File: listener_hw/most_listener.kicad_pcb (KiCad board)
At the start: 2 copper layers, 125 x 80 mm, 153 parts, among them J1 1-1394640-1, J2 ANALYSER, J3 I2S, J4 VBAT_IN, J5 PLR135/T10, J6 PLT133/T10W, J7 RCA 75R, J8 LINE L, J9 LINE R, M1 Tang Nano 20K, M2 ESP32-DevKitC-VIE, U1 74LVC1G34, U10 TPS2553DBVR, U11 74LVC1G123, U12 DIR9001, U13 SRC4192, U14 LP5907MFX-3.3, U15 PCM5102A, U16 LP5907MFX-3.3, U2 74LVC1G157, U3 74LVC1G125, U4 74LVC1G123, U5 TPS7B8133DRV, U6 LMR38020F, U7 Si514, U8 LP5907MFX-3.3, U9 74LVC1G79, X1 24.576MHz

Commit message: Board v1.3: the TOSLINK input's AUDIO flag to the host and the ASRC's RDY to its MUTE; the audio-in source chosen by itself
- firmware: the source picks itself (components/mostctl/ain): the phone while it streams,
  otherwise the TOSLINK input once its receiver has held lock on PCM for 1 s; a parity
  error's blip is kept, 100 ms of ERROR loses it; its lock time runs while the phone plays;
  key i gone
- the DIR9001 passes non-PCM (AC-3, DTS) to DOUT untouched (SLES198A 8.3.9.2): its AUDIO pin,
  channel-status bit 1, now reaches M2 IO27 (OPT_NPCM, pulled up); high drops the TOSLINK input
  at the first reading, and the console says to set the source to PCM
- the SRC4192's RDY drives its MUTE, which no longer sits on ground (SBFS022C 7.3.5): silent
  while its rate estimator settles on a new rate
- sheet: AUDIO on U12's left side, MUTE on U13's right side under RDY; the host block's text
  fitted into its frame; J5's value moved clear of OPT_NPCM; rev 1.3
- board: pads from the sheet, U13.14's ground via gone; RDY-MUTE one jumper, 1.4 mm under U13
  across RST_AIN; OPT_NPCM from U12.1 to M2.11 with three - 1.0 and 1.4 mm at M2, whose pad 11
  is walled in by I2S_DIN2_F and SRC_LRCK_F, and 3.8 mm at U12 across OPT_ERR and RST_AIN;
  37 jumpers, 83 mm in all, the longest still 6.8 mm; "v1.3" in the silk
- checks: DRC no error, no warning, nothing unconnected, matches the sheet; ERC clean; the
  firmware's pins agree with the netlist; host tests (seven broken variants of ain.c each
  caught); ESP-IDF build 979 KB, no warnings; check_all --quick 24/24

Co-Authored-By: Claude Opus 5.5 <noreply@anthropic.com>
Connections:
- M2 pad 11: unconnected-(M2-IO27-Pad11) -> /OPT_NPCM
- U12 pad 1: unconnected-(U12-AUDIO-Pad1) -> /OPT_NPCM
- U13 pad 14: GND -> Net-(U13-MUTE)
- U13 pad 15: unconnected-(U13-RDY-Pad15) -> Net-(U13-MUTE)
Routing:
- net /OPT_NPCM: track 0.00 -> 24.3 mm, vias 0 -> 5
- net Net-(U13-MUTE): track 0.00 -> 5.86 mm, vias 0 -> 2
- net GND: track 153.3 -> 152.2 mm, vias 336 -> 335
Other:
- board text added: "v1.3"
- board text removed: "v1.2"
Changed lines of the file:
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@@
 		(title "MOST25 to AUDIO: listener board")
 		(date "2026-09-28")
-		(rev "1.2")
+		(rev "1.3")
 		(comment 1 "Generated sheet: listener_hw/gen_listener.py")
 	)
@@
 			(layers "*.Cu" "*.Mask")
 			(remove_unused_layers no)
-			(net "unconnected-(M2-IO27-Pad11)")
+			(net "/OPT_NPCM")
 		)
 		(pad "12" thru_hole circle
@@
 			(layers "F.Cu" "F.Mask" "F.Paste")
 			(roundrect_rratio 0.25)
-			(net "unconnected-(U12-AUDIO-Pad1)")
+			(net "/OPT_NPCM")
 		)
 		(pad "2" smd roundrect
@@
 			(layers "F.Cu" "F.Mask" "F.Paste")
 			(roundrect_rratio 0.25)
-			(net "GND")
+			(net "Net-(U13-MUTE)")
 		)
 		(pad "15" smd roundrect
@@
 			(layers "F.Cu" "F.Mask" "F.Paste")
 			(roundrect_rratio 0.25)
-			(net "unconnected-(U13-RDY-Pad15)")
+			(net "Net-(U13-MUTE)")
 		)
 		(pad "16" smd roundrect
@@
 		)
 	)
-	(gr_text "v1.2"
+	(gr_text "v1.3"
 		(at 112.5 3.2 0)
 		(layer "F.SilkS")
@@
 	)
 	(segment
-		(start 95.75 18.775)
-		(end 96.490049 17.881654)
-		(width 0.35)
-		(locked yes)
-		(layer "F.Cu")
-		(net "GND")
-	)
-	(segment
 		(start 9 10)
 		(end 10.4 10)
@@
 	)
 	(via
-		(at 96.490049 17.881654)
-		(size 0.6)
-		(drill 0.3)
-		(layers "F.Cu" "B.Cu")
-		(locked yes)
-		(net "GND")
-	)
-	(via
 		(at 100.199999 14.2)
 		(size 0.6)
@@
 	)
 	(segment
+		(start 86.1 19.8)
+		(end 86.1 16.6)
+		(width 0.25)
+		(locked yes)
+		(layer "F.Cu")
+		(net "/OPT_NPCM")
+	)
+	(segment
+		(start 85.4 22)
+		(end 85.4 20.9)
+		(width 0.25)
+		(locked yes)
+		(layer "F.Cu")
+		(net "/OPT_NPCM")
+	)
+	(segment
+		(start 99.1 16.1)
+		(end 99.6 16.6)
+		(width 0.25)
+		(locked yes)
+		(layer "F.Cu")
+		(net "/OPT_NPCM")
+	)
+	(segment
+		(start 99.6 16.6)
+		(end 99.9 16.6)
+		(width 0.25)
+		(locked yes)
+		(layer "F.Cu")
+		(net "/OPT_NPCM")
+	)
+	(segment
+		(start 98.5 14.9)
+		(end 99.1 15.5)
+		(width 0.25)
+		(locked yes)
+		(layer "F.Cu")
+		(net "/OPT_NPCM")
+	)
+	(segment
+		(start 86.1 16.6)
+		(end 89.9 12.8)
+		(width 0.25)
+		(locked yes)
+		(layer "F.Cu")
+		(net "/OPT_NPCM")
+	)
+	(segment
+		(start 95 12.8)
+		(end 95.4 13.2)
+		(width 0.25)
+		(locked yes)
+		(layer "F.Cu")
+		(net "/OPT_NPCM")
+	)
+	(segment
+		(start 99.1 15.5)
+		(end 99.1 16.1)
+		(width 0.25)
+		(locked yes)
+		(layer "F.Cu")
+		(net "/OPT_NPCM")
+	)
+	(segment
+		(start 89.9 12.8)
+		(end 95 12.8)
+		(width 0.25)
+		(locked yes)
+		(layer "F.Cu")
+		(net "/OPT_NPCM")
+	)
+	(segment
+		(start 85.2 22.2)
+		(end 85.4 22)
+		(width 0.25)
+		(locked yes)
+		(layer "F.Cu")
+		(net "/OPT_NPCM")
+	)
+	(via
+		(at 98.5 14.9)
+		(size 0.6)
+		(drill 0.3)
+		(layers "F.Cu" "B.Cu")
+		(locked yes)
+		(net "/OPT_NPCM")
+	)
+	(via
+		(at 85.4 20.9)
+		(size 0.6)
+		(drill 0.3)
+		(layers "F.Cu" "B.Cu")
+		(locked yes)
+		(net "/OPT_NPCM")
+	)
+	(via
+		(at 86.1 19.8)
+		(size 0.6)
+		(drill 0.3)
+		(layers "F.Cu" "B.Cu")
+		(locked yes)
+		(net "/OPT_NPCM")
+	)
+	(via
+		(at 85.2 22.2)
+		(size 0.6)
+		(drill 0.3)
+		(layers "F.Cu" "B.Cu")
+		(locked yes)
+		(net "/OPT_NPCM")
+	)
+	(via
+		(at 95.4 13.2)
+		(size 0.6)
+		(drill 0.3)
+		(layers "F.Cu" "B.Cu")
+		(locked yes)
+		(net "/OPT_NPCM")
+	)
+	(segment
+		(start 84.5 22.9)
+		(end 85.2 22.2)
+		(width 0.25)
+		(locked yes)
+		(layer "B.Cu")
+		(net "/OPT_NPCM")
+	)
+	(segment
+		(start 85.4 20.5)
+		(end 86.1 19.8)
+		(width 0.25)
+		(locked yes)
+		(layer "B.Cu")
+		(net "/OPT_NPCM")
+	)
+	(segment
+		(start 85.4 20.9)
+		(end 85.4 20.5)
+		(width 0.25)
+		(locked yes)
+		(layer "B.Cu")
+		(net "/OPT_NPCM")
+	)
+	(segment
+		(start 95.4 13.2)
+		(end 97.1 14.9)
+		(width 0.25)
+		(locked yes)
+		(layer "B.Cu")
+		(net "/OPT_NPCM")
+	)
+	(segment
+		(start 97.1 14.9)
+		(end 98.5 14.9)
+		(width 0.25)
+		(locked yes)
+		(layer "B.Cu")
+		(net "/OPT_NPCM")
+	)
+	(segment
 		(start 86.0412 11.4948)
 		(end 84.074 13.462)
@@
 		(net "Net-(U13-RCKI)")
 	)
+	(segment
+		(start 92.3 18.7)
+		(end 92.2 18.6)
+		(width 0.25)
+		(locked yes)
+		(layer "F.Cu")
+		(net "Net-(U13-MUTE)")
+	)
+	(segment
+		(start 90.6 18.9)
+		(end 89.6 18.9)
+		(width 0.25)
+		(locked yes)
+		(layer "F.Cu")
+		(net "Net-(U13-MUTE)")
+	)
+	(segment
+		(start 91.2 19.5)
+		(end 90.6 18.9)
+		(width 0.25)
+		(locked yes)
+		(layer "F.Cu")
+		(net "Net-(U13-MUTE)")
+	)
+	(segment
+		(start 94.8 18.7)
+		(end 92.3 18.7)
+		(width 0.25)
+		(locked yes)
+		(layer "F.Cu")
+		(net "Net-(U13-MUTE)")
+	)
+	(via
+		(at 91.2 19.5)
+		(size 0.6)
+		(drill 0.3)
+		(layers "F.Cu" "B.Cu")
+		(locked yes)
+		(net "Net-(U13-MUTE)")
+	)
+	(via
+		(at 92.2 18.6)
+		(size 0.6)
+		(drill 0.3)
+		(layers "F.Cu" "B.Cu")
+		(locked yes)
+		(net "Net-(U13-MUTE)")
+	)
+	(segment
+		(start 92.1 18.6)
+		(end 91.2 19.5)
+		(width 0.25)
+		(locked yes)
+		(layer "B.Cu")
+		(net "Net-(U13-MUTE)")
+	)
+	(segment
+		(start 92.2 18.6)
+		(end 92.1 18.6)
+		(width 0.25)
+		(locked yes)
+		(layer "B.Cu")
+		(net "Net-(U13-MUTE)")
+	)
 	(zone

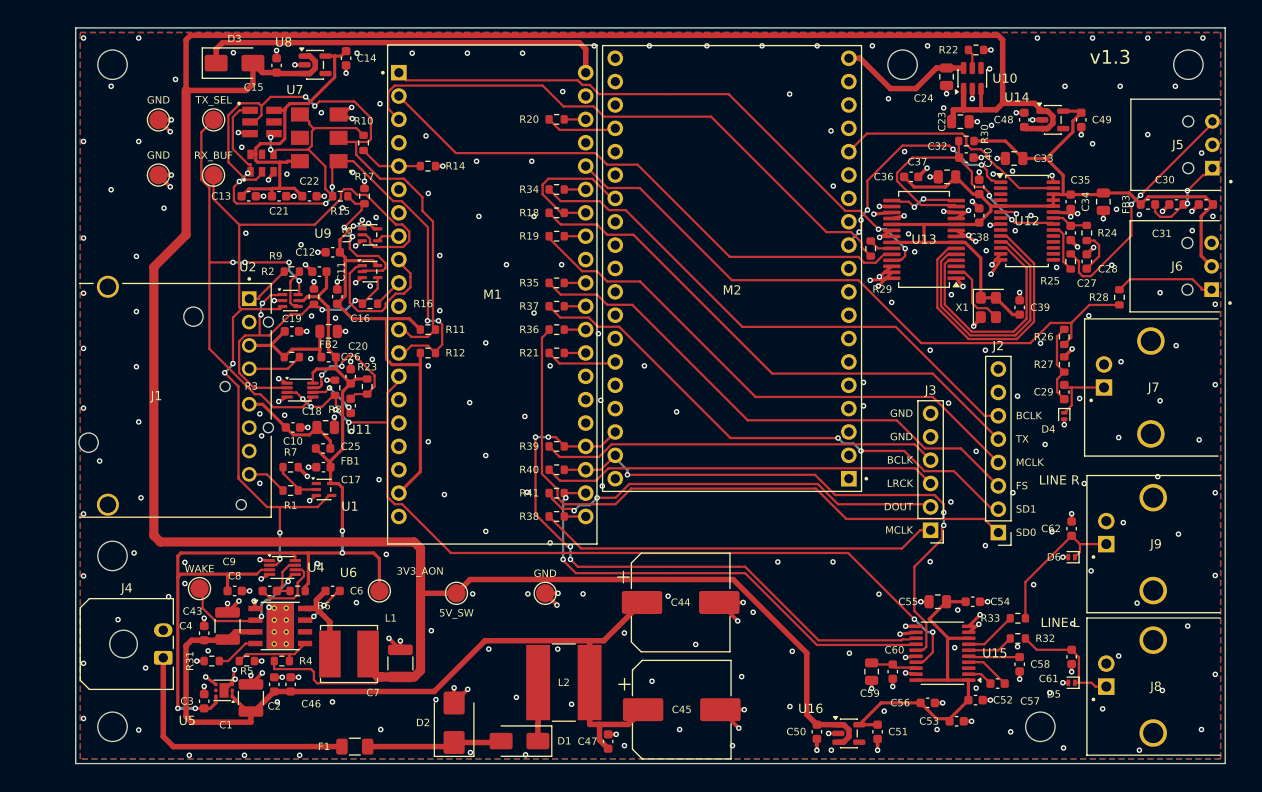
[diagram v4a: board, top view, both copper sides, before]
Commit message: Board v1.4: placed again by hand and routed again - 11 jumpers instead of 37; the line out buffered by an OPA1678
The user re-placed the board group by group - the ring and clock cluster round
J1, the S/PDIF group (U12, U13), the DAC, the power corner - and every round was
routed again on top: 37 jumpers became 11, 83 mm of bottom copper 29, vias 407
became 300. The 11 left are short (5.3 mm at most) and sit where pin orders or a
walled pin leave no way on top.

Line out (block 11): U17, an OPA1678 on 5V_SW and VNEG_A (-5.2 V from U18, a
TPS60403), makes a unity-gain Sallen-Key low-pass per channel - R32/R33 and
R43/R44 4k7, C69/C70 820p, C71/C72 390p: 60 kHz, Q 0.72 - then 100R, 2n2 and the
ESD diode at each jack. At +-5 V an NE5532 or TL072 cannot take the PCM5102A's
2.1 Vrms at its inputs; the OPA1678's inputs reach V-. On one layer the dual
needs two crossings: 5V_SW passes between R45's pads, VNEG_A under U17's body.

3V3_DAC runs on top now (its jumper gone), and 5V_SW comes beside it to the
buffer, with 100u + 100n (C78, C79) at its end. The 5 V trunk got 100u + 100n
by D3 (C63, C64) and four more 100n along it (C65-C68). R3 is two 27k in
parallel (R3, R42). The Si514 land pattern takes the 3.2x5 and 2.5x3.2 packages
only. TP1, TP3, TP8 and TP10 are gone, and 20 two-pad parts were turned.

DRC: no error, nothing unconnected, the board matches the sheet; ERC clean.
Warnings are silk only: references overlapping a pad or another reference.

Co-Authored-By: Claude Opus 5.5 <noreply@anthropic.com>
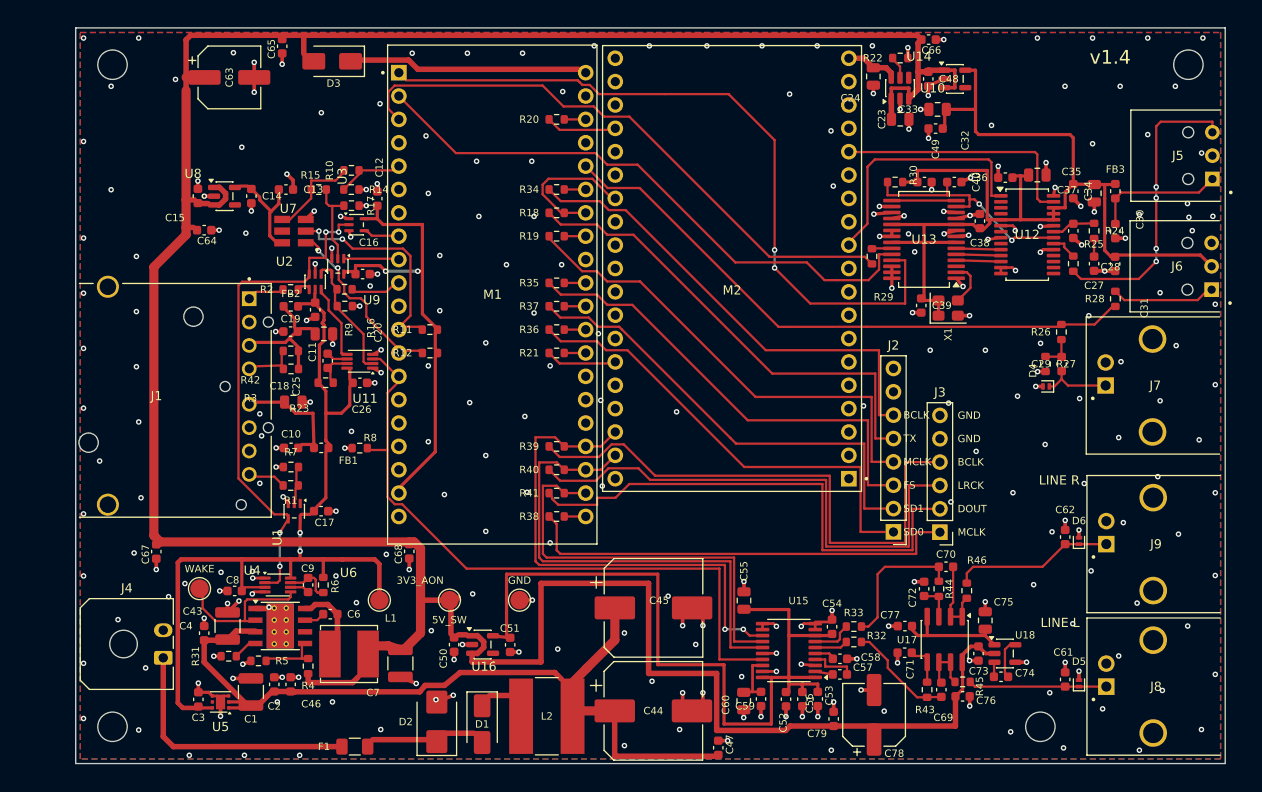
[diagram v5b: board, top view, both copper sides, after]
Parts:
- removed C21, C22: 100n, Capacitor_SMD:C_0603_1608Metric
- removed H5, H6: M3, MountingHole_3.2mm_M3
- removed TP1: RX_BUF, TestPoint:TestPoint_Pad_D2.0mm
- removed TP10, TP8: GND, TestPoint:TestPoint_Pad_D2.0mm
- removed TP3: TX_SEL, TestPoint:TestPoint_Pad_D2.0mm
- added C63: 100u 16V, Capacitor_SMD:CP_Elec_6.3x7.7, F.Cu at (16.7, 5.38)
- added C64: 100n, Capacitor_SMD:C_0603_1608Metric, F.Cu at (14.0, 22.0)
- added C65: 100n, Capacitor_SMD:C_0603_1608Metric, F.Cu at (22.5, 1.99)
- added C66: 100n, Capacitor_SMD:C_0603_1608Metric, F.Cu at (92.7, 1.27)
- added C67: 100n, Capacitor_SMD:C_0603_1608Metric, F.Cu at (8.76, 56.9)
- added C68: 100n, Capacitor_SMD:C_0603_1608Metric, F.Cu at (36.3, 56.9)
- added C69: 820p, Capacitor_SMD:C_0603_1608Metric, F.Cu at (94.1, 72.0)
- added C70: 820p, Capacitor_SMD:C_0603_1608Metric, F.Cu at (94.6, 58.6)
- added C71: 390p, Capacitor_SMD:C_0603_1608Metric, F.Cu at (90.1, 67.9)
- added C72: 390p, Capacitor_SMD:C_0603_1608Metric, F.Cu at (92.3, 61.0)
- added C73: 1u, Capacitor_SMD:C_0603_1608Metric, F.Cu at (98.2, 68.0)
- added C74: 1u, Capacitor_SMD:C_0603_1608Metric, F.Cu at (100.6, 70.6)
- added C75: 4u7, Capacitor_SMD:C_0805_2012Metric, F.Cu at (98.9, 64.4)
- added C76: 100n, Capacitor_SMD:C_0603_1608Metric, F.Cu at (96.4, 72.7)
- added C77: 100n, Capacitor_SMD:C_0603_1608Metric, F.Cu at (90.2, 65.0)
- added C78: 100u 16V, Capacitor_SMD:CP_Elec_6.3x7.7, F.Cu at (86.8, 74.7)
- added C79: 100n, Capacitor_SMD:C_0603_1608Metric, F.Cu at (82.4, 75.1)
- added R42: 27k, Resistor_SMD:R_0603_1608Metric, F.Cu at (23.4, 35.1)
- added R43: 4k7, Resistor_SMD:R_0603_1608Metric, F.Cu at (92.6, 72.0)
- added R44: 4k7, Resistor_SMD:R_0603_1608Metric, F.Cu at (93.9, 61.0)
- added R45: 100, Resistor_SMD:R_0603_1608Metric, F.Cu at (96.4, 71.1)
- added R46: 100, Resistor_SMD:R_0603_1608Metric, F.Cu at (96.9, 61.2)
- added U17: OPA1678, Package_SO:SOIC-8_3.9x4.9mm_P1.27mm, F.Cu at (94.5, 66.5)
- added U18: TPS60403, Package_TO_SOT_SMD:SOT-23-5, F.Cu at (101.0, 68.0)
- R3: value 13k7 1% -> 27k
- R32, R33: value 470 -> 4k7
- U7: footprint most_listener:Si514_5x7_3.2x5_2.5x3.2 -> most_listener:Si514_3.2x5_2.5x3.2
- moved C51 41.1 mm to (47.2, 67.1)
- moved U16 41.0 mm to (44.2, 67.1)
- moved C50 40.6 mm to (41.1, 67.1)
- moved C55 21.1 mm to (72.7, 62.3), turned to 90 degrees
- moved C58 19.6 mm to (83.1, 68.6), turned to 0 degrees
- moved C52 18.8 mm to (79.0, 73.0), turned to -90 degrees
- moved C14 18.2 mm to (19.1, 18.3)
- moved R33 17.9 mm to (84.6, 65.1)
- moved R32 17.8 mm to (84.6, 66.8)
- moved U8 17.4 mm to (16.2, 18.3)
- moved C57 17.2 mm to (83.1, 70.3)
- moved U15 16.7 mm to (77.6, 67.7)
- moved C15 16.6 mm to (13.3, 18.3)
- moved C49 15.9 mm to (93.5, 10.9), turned to 180 degrees
- moved C54 15.5 mm to (82.2, 65.1), turned to 90 degrees
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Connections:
- R32 pad 2: Net-(D5-A1) -> Net-(C69-Pad1)
- R33 pad 2: Net-(D6-A1) -> Net-(C70-Pad1)
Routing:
- net 3V3_DAC: track 39.1 -> 88.4 mm
- net /TX_SEL: track 52.6 -> 8.44 mm, vias 4 -> 0
- net /SI_SCL: track 62.1 -> 22.5 mm
- net /SI_SDA: track 57.6 -> 18.3 mm, vias 6 -> 2
- net /RX_BUF: track 88.9 -> 55.2 mm
- net Net-(U7-VDD): track 37.4 -> 9.99 mm
- net Net-(U12-LRCKO): track 31.7 -> 4.86 mm
- net Net-(U12-BCKO): track 28.8 -> 4.86 mm
- net /TX_REGEN: track 35.2 -> 12.0 mm, vias 4 -> 0
- net /LOCK: track 94.4 -> 71.3 mm, vias 6 -> 0
- net Net-(U12-DOUT): track 25.8 -> 4.86 mm
- net Net-(D3-K): track 44.9 -> 24.0 mm
- net 3V3_AON: track 109.5 -> 89.6 mm, vias 4 -> 2
- net Net-(J2-SD0): track 68.6 -> 50.7 mm
- net Net-(J3-BCLK): track 43.2 -> 61.0 mm
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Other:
- board text added: "v1.4"
- board text removed: "v1.3"

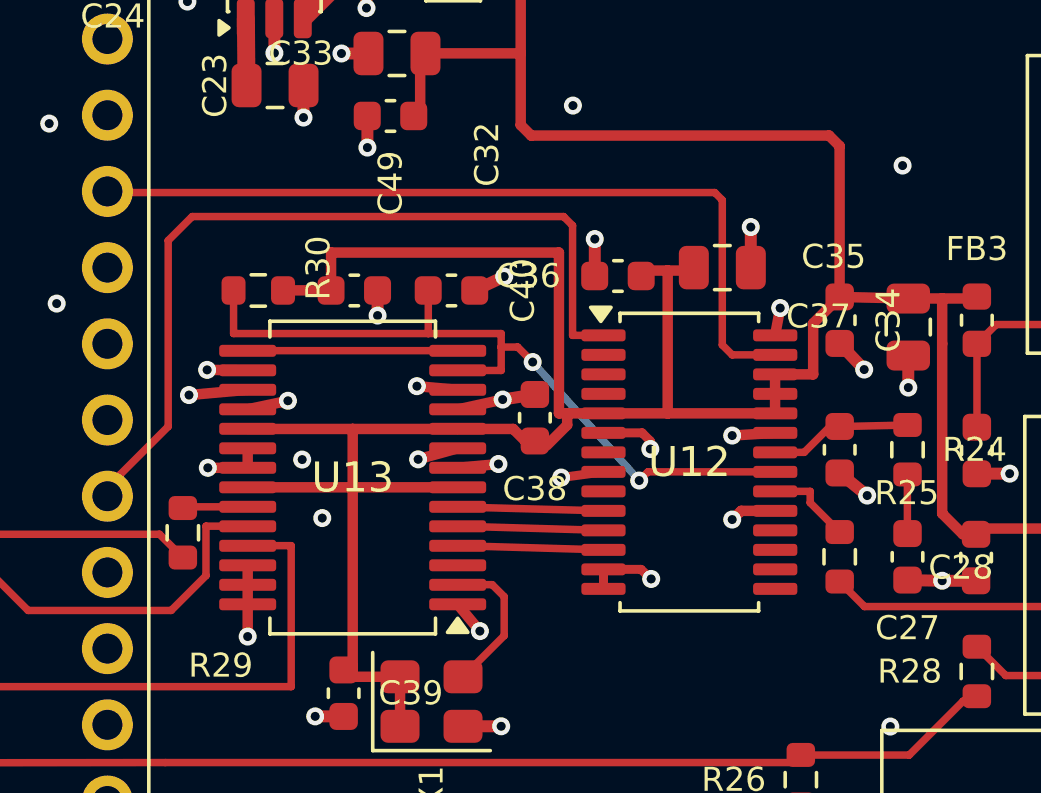
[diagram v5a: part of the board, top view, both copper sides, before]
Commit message: Board v1.4: RST_AIN's jumper 3.4 mm instead of 5.3 after the user raised U12 and C38; the modules' sockets in the 3D view
The user raised U12 by 0.26 mm and moved C38 to the top of the gap between U13
and U12. RST_AIN now runs down that gap and crosses under U12's left row at pin
9 (not connected) into the body: 3.4 mm of bottom copper instead of 5.3. U12's
copper follows its pads; its outputs to U13 run straight across.

U13's 3V3_DA (pins 7, 10, 19, 22, X1, C39) reached the supply only over that
gap, from U12.5 past C38's old place, which RST_AIN would now cross. It is fed
from the left instead: the trunk at y 15.5 goes on past R30 and down beside
U13's left row into pin 19. U13.16/17's GND vias there went; 16-17-18 are joined
at their pads and share 18's via. The labels of C36, C37, C38 and C40 moved off
the parts that now sit under them.

M1 and M2 carry KiCad's 1x20 / 1x19 socket models under their rows (2.54 mm,
8.5 mm high, soldered to the board), as J2 and J3 show their headers.

11 jumpers, 27 mm, the longest 3.7 mm. DRC: no error, nothing unconnected, the
board matches the sheet; lint adds nothing.

Co-Authored-By: Claude Opus 5.5 <noreply@anthropic.com>
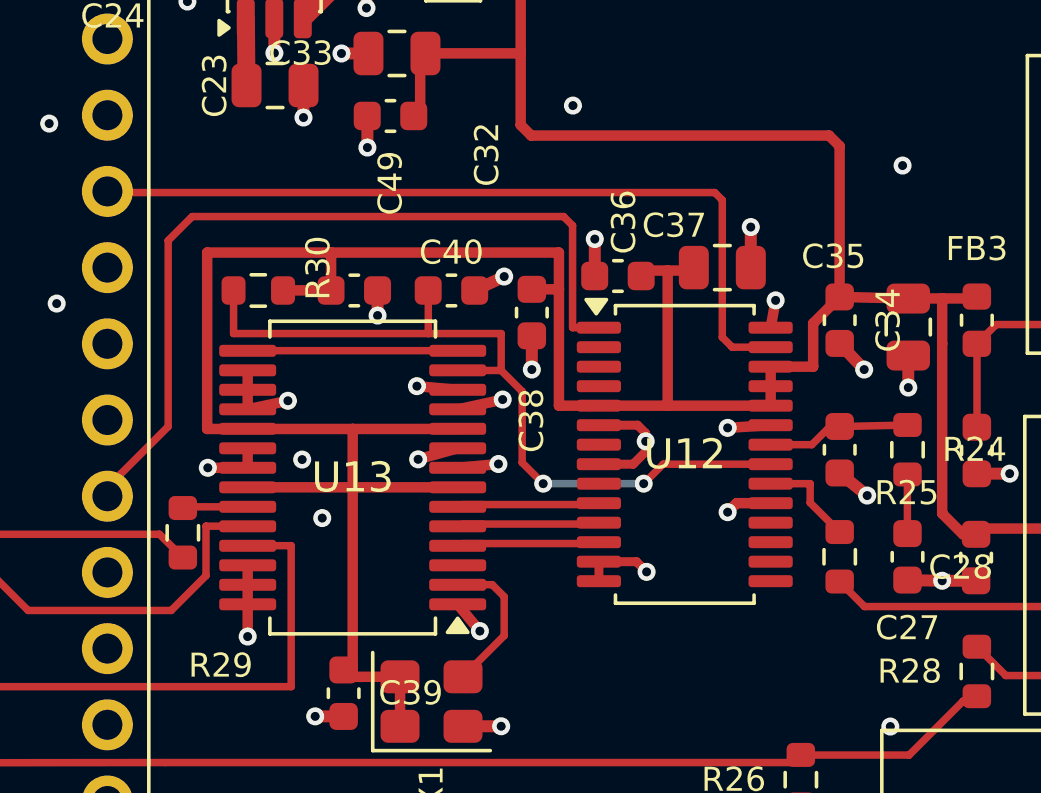
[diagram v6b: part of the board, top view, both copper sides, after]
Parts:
- moved C38 3.51 mm to (98.2, 17.5), turned to -90 degrees
- moved U12 0.30 mm to (103.3, 22.2)
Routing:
- net 3V3_DA: track 118.1 -> 125.6 mm
- net GND: track 149.5 -> 148.3 mm, vias 278 -> 276
- net /RST_AIN: track 25.7 -> 26.7 mm
